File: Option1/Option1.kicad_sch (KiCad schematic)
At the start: 0 parts

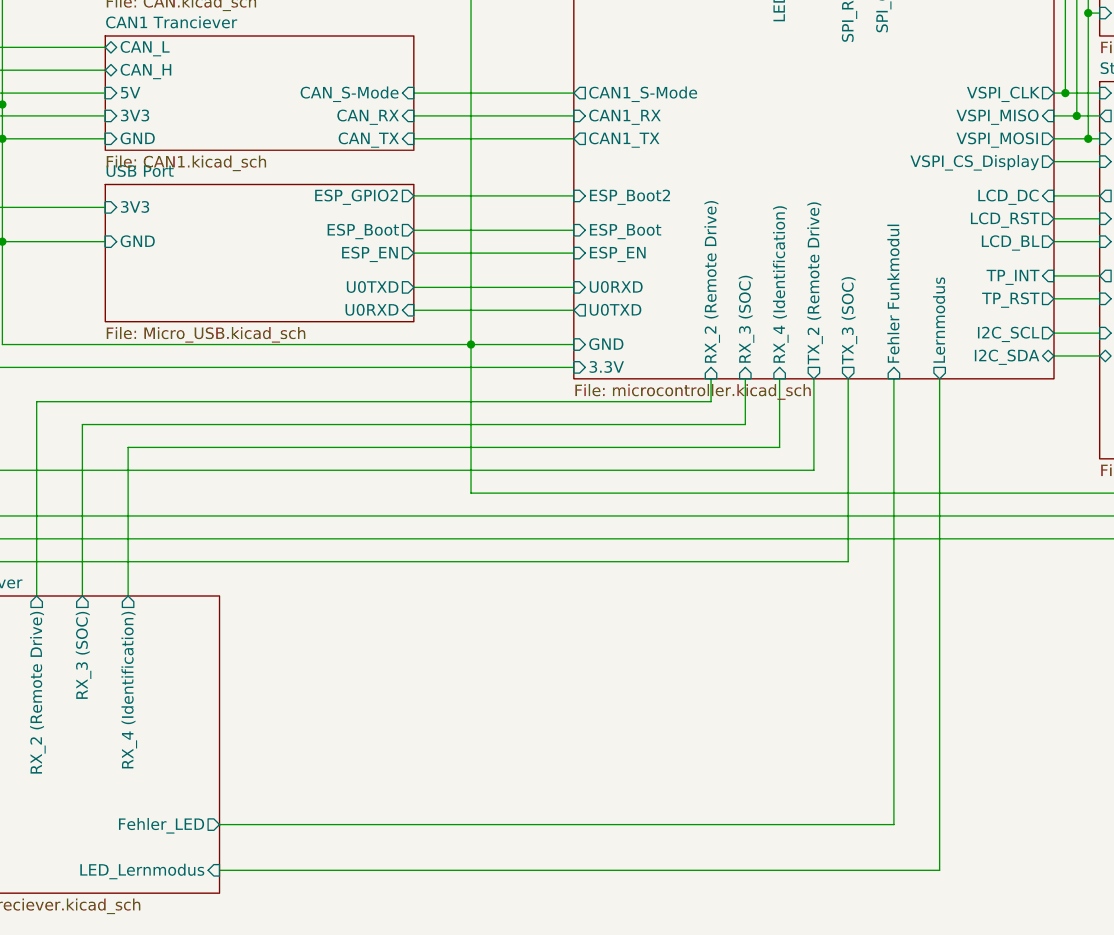
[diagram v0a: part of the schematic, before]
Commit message: EasyEDA Lib in Projekt verschoben; Footprints, Silkscreen für designrule angepasst; Bauteilbeschriftungen entfernt, müssen neu angeordnet werden, JLC Rules eingebunden, Designrules erfolgreich bis auf Beschriftungen, Fehler in Radio Controll Beschaltung behoben; RFID Pinheader hinzugefügt
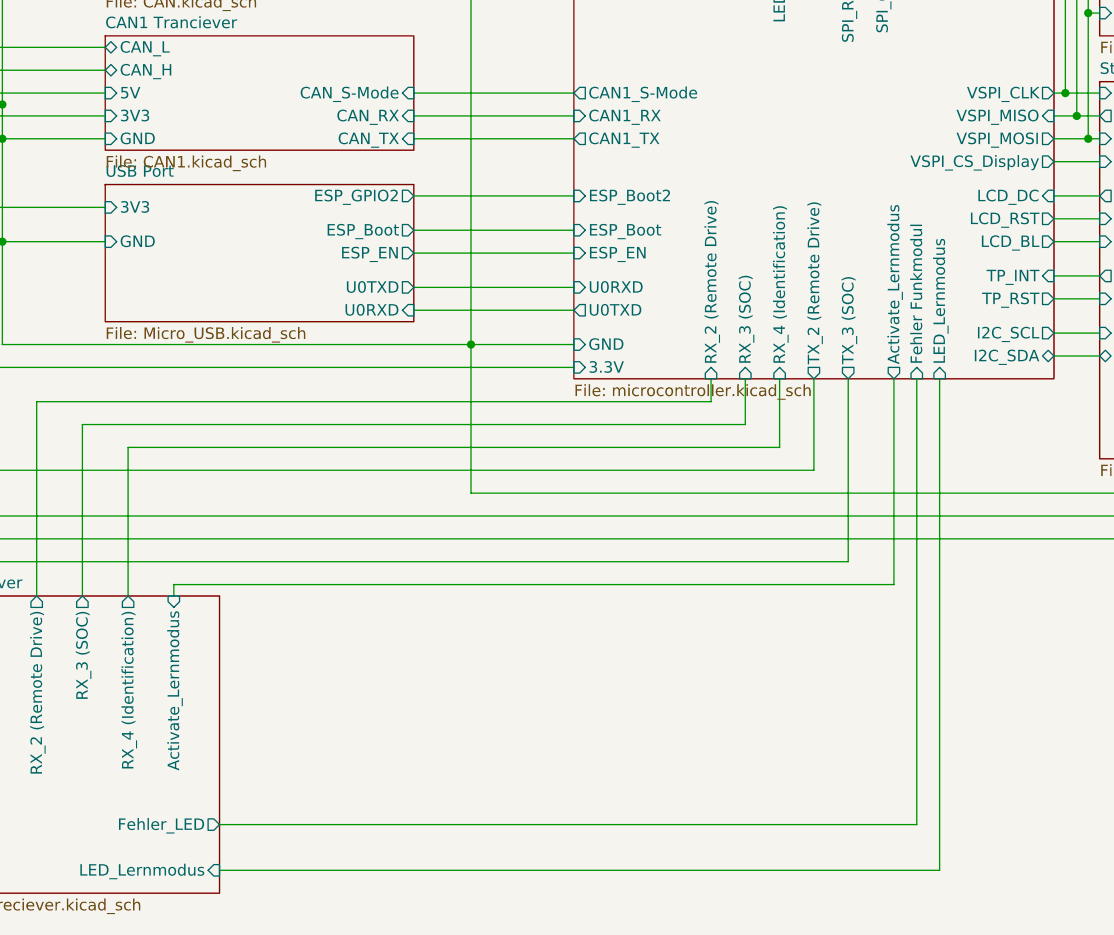
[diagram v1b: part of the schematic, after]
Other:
- sheet Funk Reciever ports: added Activate_Lernmodus; removed none
- sheet MCT  Wlan ports: added Activate_Lernmodus, LED_Lernmodus; removed Lernmodus
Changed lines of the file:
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@@
 	(wire
 		(pts
-			(xy 241.3 102.87) (xy 241.3 152.4)
+			(xy 243.84 102.87) (xy 243.84 152.4)
 		)
 		(stroke
@@
 	(wire
 		(pts
+			(xy 161.29 125.73) (xy 241.3 125.73)
+		)
+		(stroke
+			(width 0)
+			(type default)
+		)
+	)
+	(wire
+		(pts
 			(xy 262.89 35.56) (xy 262.89 50.8)
 		)
@@
 	(wire
 		(pts
-			(xy 166.37 152.4) (xy 241.3 152.4)
+			(xy 166.37 152.4) (xy 243.84 152.4)
 		)
 		(stroke
@@
 	(wire
 		(pts
+			(xy 161.29 127) (xy 161.29 125.73)
+		)
+		(stroke
+			(width 0)
+			(type default)
+		)
+	)
+	(wire
+		(pts
 			(xy 187.96 53.34) (xy 205.74 53.34)
 		)
@@
 		(pts
 			(xy 187.96 88.9) (xy 205.74 88.9)
+		)
+		(stroke
+			(width 0)
+			(type default)
+		)
+	)
+	(wire
+		(pts
+			(xy 241.3 125.73) (xy 241.3 102.87)
 		)
 		(stroke
@@
 			)
 		)
+		(pin "Activate_Lernmodus" input
+			(at 161.29 127 90)
+			(effects
+				(font
+					(size 1.27 1.27)
+				)
+				(justify right)
+			)
+		)
 		(instances
 			(project "Option1"
@@
 			)
 		)
-		(pin "Lernmodus" output
+		(pin "LED_Lernmodus" input
 			(at 246.38 102.87 270)
 			(effects
@@
 		)
 		(pin "Fehler Funkmodul" input
-			(at 241.3 102.87 270)
+			(at 243.84 102.87 270)
 			(effects
 				(font
@@
 			(effects
 				(font
+					(size 1.27 1.27)
+				)
+				(justify left)
+			)
+		)
+		(pin "Activate_Lernmodus" output
+			(at 241.3 102.87 270)
+			(effects
+				(font

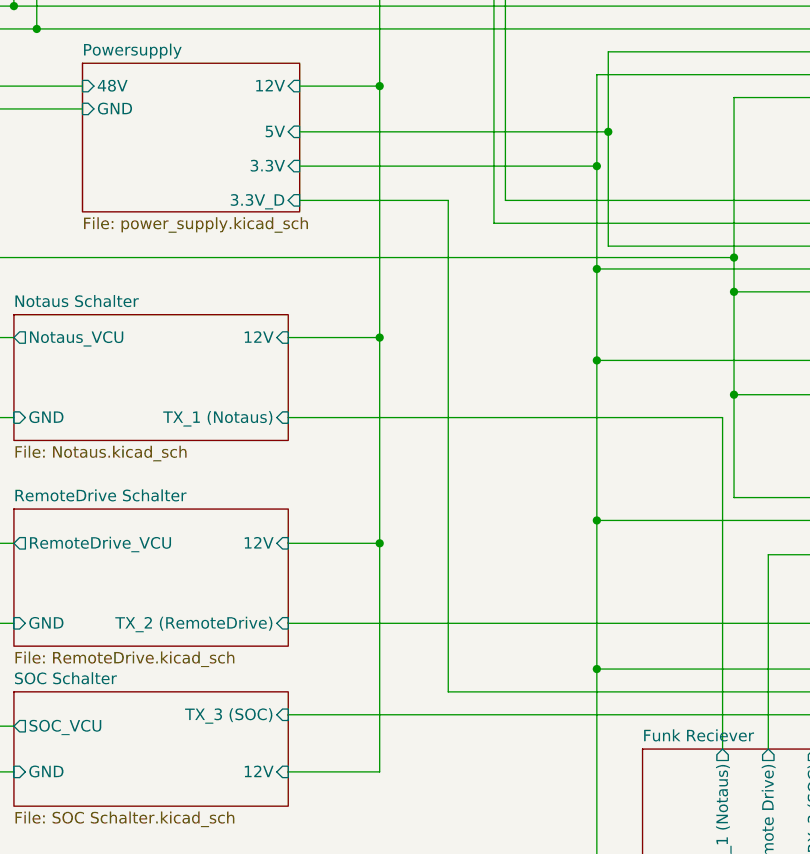
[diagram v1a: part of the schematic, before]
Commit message: Platine korrigeiert, 5V DCDC getauscht, 3.3V Display Versorgung entfernt. Bauteile neu angeordnet, USB 5V auf 5V Supply geführt
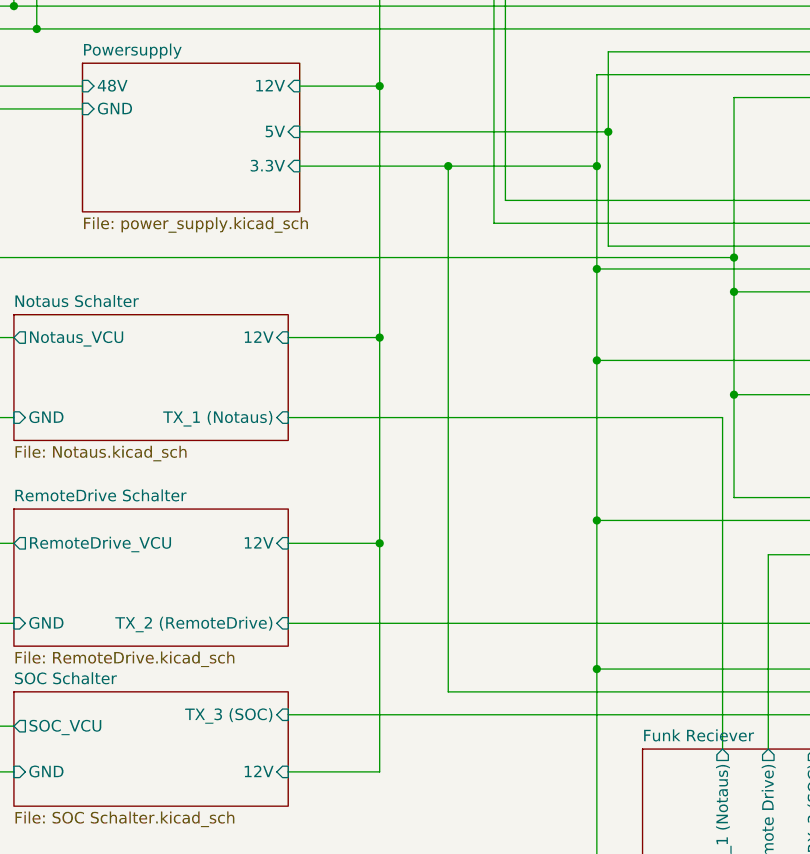
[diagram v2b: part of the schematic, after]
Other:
- sheet Powersupply ports: added none; removed 3.3V_D
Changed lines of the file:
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@@
 	)
 	(junction
+		(at 110.49 62.23)
+		(diameter 0)
+		(color 0 0 0 0)
+	)
+	(junction
 		(at 127 62.23)
 		(diameter 0)
@@
 	(wire
 		(pts
-			(xy 93.98 66.04) (xy 110.49 66.04)
-		)
-		(stroke
-			(width 0)
-			(type default)
-			(color 255 137 135 1)
-		)
-	)
-	(wire
-		(pts
 			(xy 127 83.82) (xy 127 101.6)
 		)
@@
 	(wire
 		(pts
-			(xy 93.98 62.23) (xy 127 62.23)
+			(xy 93.98 62.23) (xy 110.49 62.23)
 		)
 		(stroke
@@
 	(wire
 		(pts
+			(xy 110.49 62.23) (xy 127 62.23)
+		)
+		(stroke
+			(width 0)
+			(type default)
+			(color 255 137 135 1)
+		)
+	)
+	(wire
+		(pts
 			(xy 102.87 81.28) (xy 92.71 81.28)
 		)
@@
 	(wire
 		(pts
-			(xy 110.49 66.04) (xy 110.49 120.65)
+			(xy 110.49 62.23) (xy 110.49 120.65)
 		)
 		(stroke
@@
 			(effects
 				(font
-					(size 1.27 1.27)
-				)
-				(justify right)
-			)
-		)
-		(pin "3.3V_D" input
-			(at 93.98 66.04 0)
-			(effects
-				(font

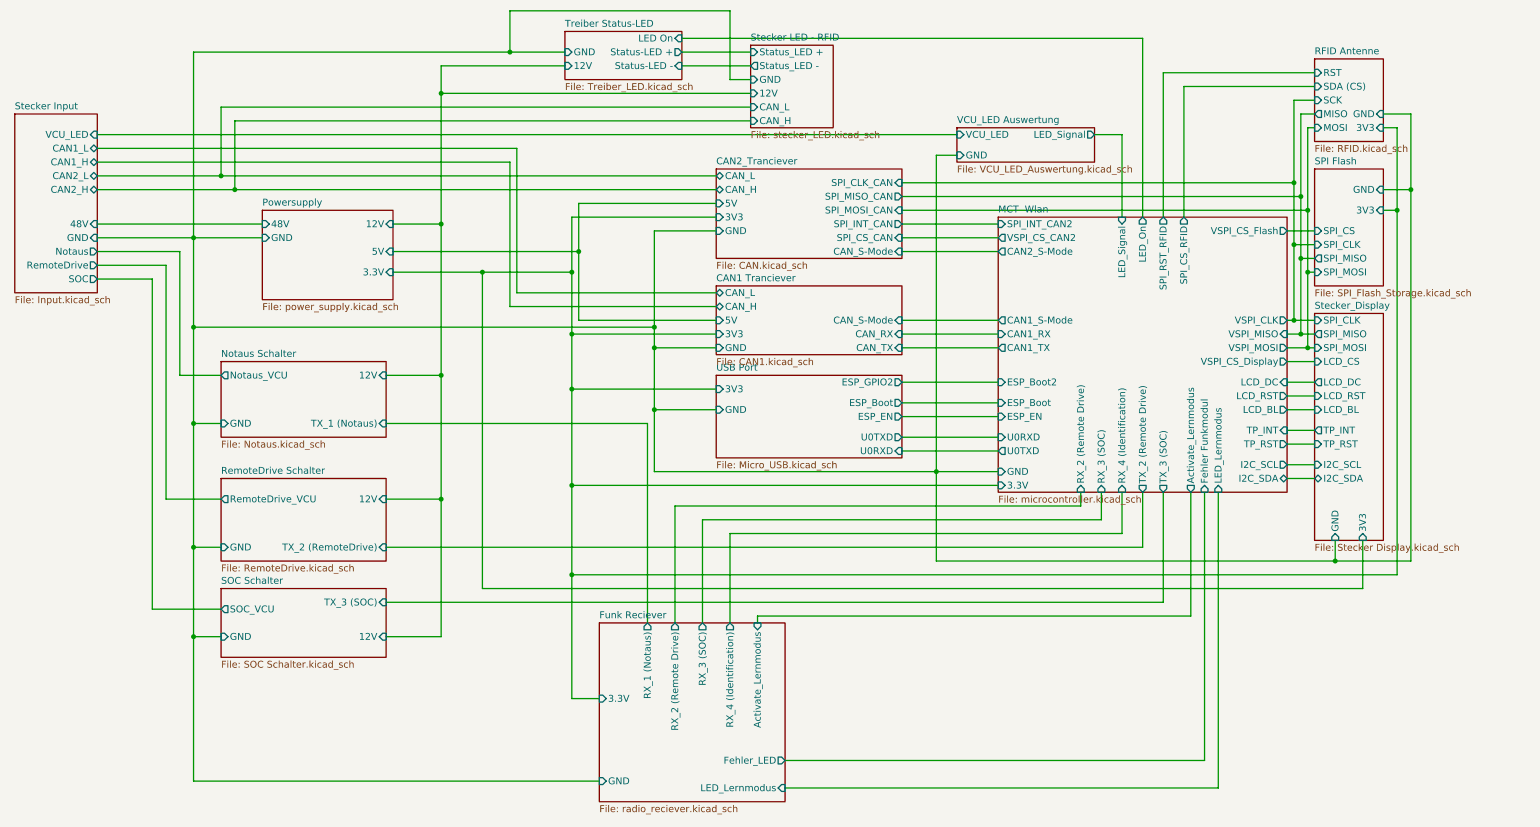
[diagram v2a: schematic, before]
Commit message: power Supply angepasst für 12V und 48V, Datenblätter für DCDCs hinzugefügt
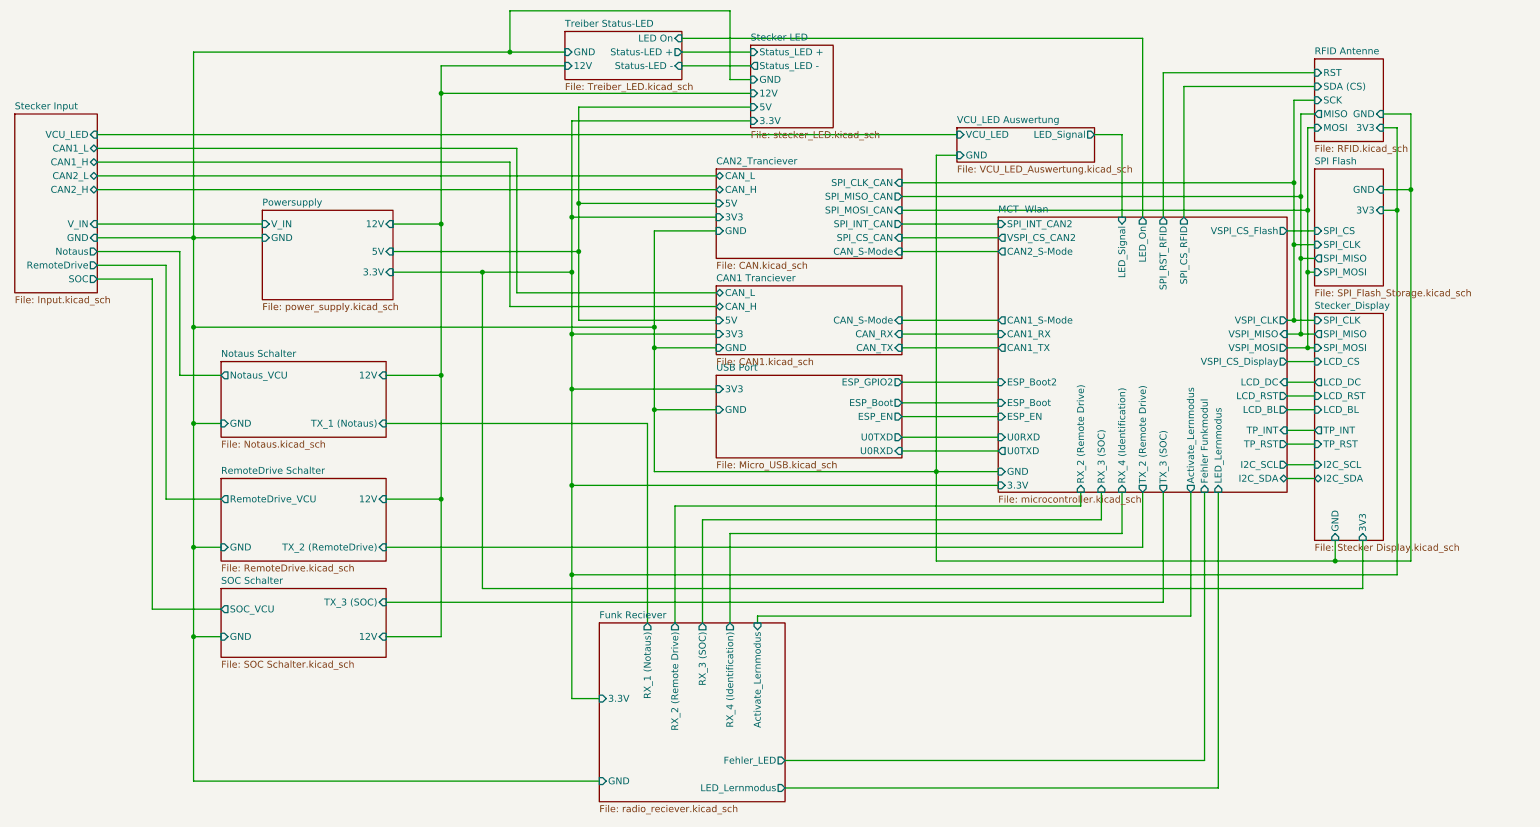
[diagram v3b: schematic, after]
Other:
- sheet Stecker LED - RFID renamed Stecker LED
- sheet Powersupply ports: added V_IN; removed 48V
- sheet Stecker Input ports: added V_IN; removed 48V
- sheet Stecker LED ports: added 3.3V, 5V; removed CAN_H, CAN_L
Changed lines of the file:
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@@
 	)
 	(junction
-		(at 62.23 44.45)
-		(diameter 0)
-		(color 194 194 194 1)
-	)
-	(junction
 		(at 57.15 90.17)
 		(diameter 0)
@@
 	)
 	(junction
+		(at 128.27 49.53)
+		(diameter 0)
+		(color 0 0 0 0)
+	)
+	(junction
+		(at 127 52.07)
+		(diameter 0)
+		(color 0 0 0 0)
+	)
+	(junction
 		(at 142.24 72.39)
 		(diameter 0)
@@
 		(color 255 0 4 1)
 	)
-	(junction
-		(at 64.77 46.99)
-		(diameter 0)
-		(color 0 0 255 1)
-	)
 	(wire
 		(pts
@@
 	(wire
 		(pts
-			(xy 62.23 124.46) (xy 49.53 124.46)
+			(xy 127 34.29) (xy 160.02 34.29)
 		)
 		(stroke
 			(width 0)
 			(type default)
+			(color 255 137 135 1)
 		)
 	)
 	(wire
 		(pts
-			(xy 62.23 31.75) (xy 160.02 31.75)
+			(xy 62.23 124.46) (xy 49.53 124.46)
 		)
 		(stroke
 			(width 0)
-			(type dash)
-			(color 194 194 194 1)
+			(type default)
 		)
 	)
@@
 	(wire
 		(pts
-			(xy 64.77 46.99) (xy 153.67 46.99)
-		)
-		(stroke
-			(width 0)
-			(type solid)
-			(color 0 0 255 1)
-		)
-	)
-	(wire
-		(pts
 			(xy 57.15 55.88) (xy 69.85 55.88)
 		)
@@
 	(wire
 		(pts
-			(xy 127 101.6) (xy 205.74 101.6)
+			(xy 128.27 31.75) (xy 160.02 31.75)
 		)
 		(stroke
-			(width 0)
+			(width 0.3)
 			(type default)
-			(color 255 137 135 1)
+			(color 255 73 88 1)
 		)
 	)
 	(wire
 		(pts
-			(xy 62.23 31.75) (xy 62.23 44.45)
+			(xy 127 101.6) (xy 205.74 101.6)
 		)
 		(stroke
 			(width 0)
-			(type dash)
-			(color 194 194 194 1)
+			(type default)
+			(color 255 137 135 1)
 		)
 	)
@@
 	(wire
 		(pts
-			(xy 127 52.07) (xy 127 62.23)
-		)
-		(stroke
-			(width 0)
-			(type default)
-			(color 255 137 135 1)
-		)
-	)
-	(wire
-		(pts
 			(xy 142.24 87.63) (xy 142.24 99.06)
 		)
@@
 	(wire
 		(pts
+			(xy 128.27 49.53) (xy 128.27 31.75)
+		)
+		(stroke
+			(width 0.3)
+			(type default)
+			(color 255 73 88 1)
+		)
+	)
+	(wire
+		(pts
+			(xy 127 52.07) (xy 127 34.29)
+		)
+		(stroke
+			(width 0)
+			(type default)
+			(color 255 137 135 1)
+		)
+	)
+	(wire
+		(pts
 			(xy 127 140.97) (xy 127 118.11)
 		)
@@
 	(wire
 		(pts
-			(xy 39.37 44.45) (xy 62.23 44.45)
+			(xy 39.37 44.45) (xy 153.67 44.45)
 		)
 		(stroke
@@
 	(wire
 		(pts
-			(xy 64.77 34.29) (xy 64.77 46.99)
-		)
-		(stroke
-			(width 0)
-			(type solid)
-			(color 0 0 255 1)
-		)
-	)
-	(wire
-		(pts
 			(xy 142.24 76.2) (xy 153.67 76.2)
 		)
@@
 	(wire
 		(pts
-			(xy 64.77 34.29) (xy 160.02 34.29)
-		)
-		(stroke
-			(width 0)
-			(type solid)
-			(color 0 0 255 1)
-		)
-	)
-	(wire
-		(pts
 			(xy 262.89 50.8) (xy 262.89 62.23)
 		)
@@
 	(wire
 		(pts
+			(xy 127 52.07) (xy 127 62.23)
+		)
+		(stroke
+			(width 0)
+			(type default)
+			(color 255 137 135 1)
+		)
+	)
+	(wire
+		(pts
 			(xy 161.29 127) (xy 161.29 125.73)
 		)
@@
 	(wire
 		(pts
-			(xy 39.37 46.99) (xy 64.77 46.99)
+			(xy 39.37 46.99) (xy 153.67 46.99)
 		)
 		(stroke
@@
 	(wire
 		(pts
-			(xy 62.23 44.45) (xy 153.67 44.45)
-		)
-		(stroke
-			(width 0)
-			(type dash)
-			(color 194 194 194 1)
-		)
-	)
-	(wire
-		(pts
 			(xy 259.08 91.44) (xy 264.16 91.44)
 		)
@@
 			)
 		)
-		(pin "LED_Lernmodus" input
-			(at 166.37 157.48 0)
-			(effects
-				(font
-					(size 1.27 1.27)
-				)
-				(justify right)
-			)
-		)
 		(pin "3.3V" input
 			(at 132.08 140.97 180)
@@
 			)
 		)
+		(pin "LED_Lernmodus" output
+			(at 166.37 157.48 0)
+			(effects
+				(font
+					(size 1.27 1.27)
+				)
+				(justify right)
+			)
+		)
 		(instances
 			(project "Option1"
@@
 			(color 102 255 255 1.0000)
 		)
-		(property "Sheetname" "Stecker LED - RFID"
+		(property "Sheetname" "Stecker LED"
 			(at 160.02 19.6084 0)
 			(effects
@@
 			)
 		)
-		(pin "CAN_L" input
-			(at 160.02 31.75 180)
+		(pin "3.3V" input
+			(at 160.02 34.29 180)
 			(effects
 				(font
@@
 			)
 		)
-		(pin "CAN_H" input
-			(at 160.02 34.29 180)
+		(pin "5V" input
+			(at 160.02 31.75 180)
 			(effects
 				(font
@@
 			)
 		)
-		(pin "48V" input
-			(at 39.37 53.34 0)
-			(effects
-				(font
-					(size 1.27 1.27)
-				)
-				(justify right)
-			)
-		)
 		(pin "GND" input
 			(at 39.37 55.88 0)
@@
 			)
 		)
+		(pin "V_IN" input
+			(at 39.37 53.34 0)
+			(effects
+				(font
+					(size 1.27 1.27)
+				)
+				(justify right)
+			)
+		)
 		(instances
 			(project "Option1"
@@
 			)
 		)
-		(pin "48V" input
-			(at 69.85 53.34 180)
-			(effects
-				(font
-					(size 1.27 1.27)
-				)
-				(justify left)
-			)
-		)
 		(pin "GND" input
 			(at 69.85 55.88 180)
@@
 			)
 		)
+		(pin "V_IN" input
+			(at 69.85 53.34 180)
+			(effects
+				(font
+					(size 1.27 1.27)
+				)
+				(justify left)
+			)
+		)
